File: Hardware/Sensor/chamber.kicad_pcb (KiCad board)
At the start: 2 copper layers, 83 x 95 mm, 106 parts, among them J1 Conn_01x16_Female, J2 Conn_01x16_Female, J3 RF_Shield_One_Piece, J4 Conn_Coaxial, J5 Conn_01x03_Male, J6 Conn_01x03_Male, J7 UART, J8 USB_B_Micro, J9 Conn_01x04, Q1 Q_PMOS_GDS, Q2 Q_PMOS_GDS, Q3 Q_NMOS_GDS, Q4 Q_NMOS_GDS, Q5 Q_NPN_BEC, Q6 Q_PMOS_GDS, Q7 Q_NMOS_GDS, Q8 Q_PMOS_GDS, Q9 Q_NMOS_GDS, SW1 UP, SW2 DOWN, SW3 LEFT, SW4 RIGHT, U1 SSD1306, U2 MCP3425A0T-ECH, U3 LMC662, U4 LM358, U5 STM8S105K4B6, Y1 Crystal

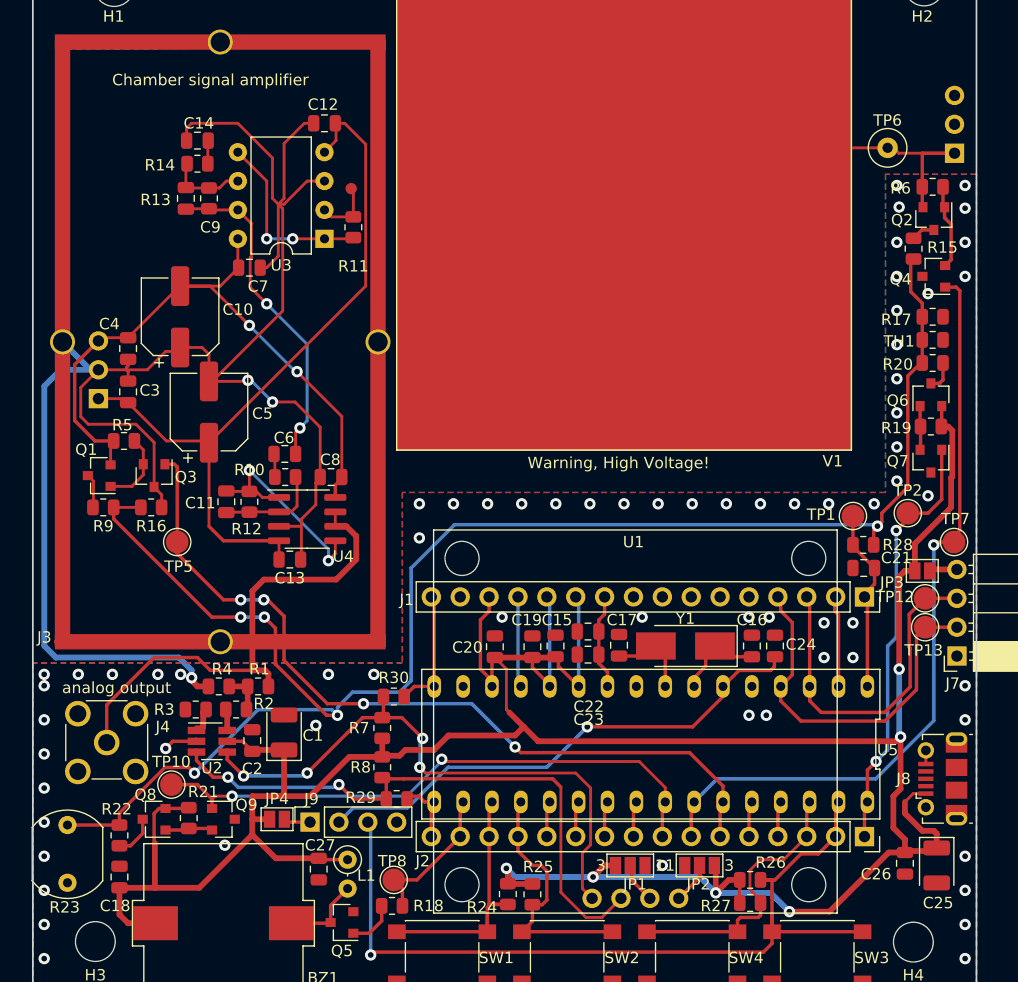
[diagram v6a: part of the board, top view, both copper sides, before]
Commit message: added references to LCSC shop (for some components), slighty improved routing
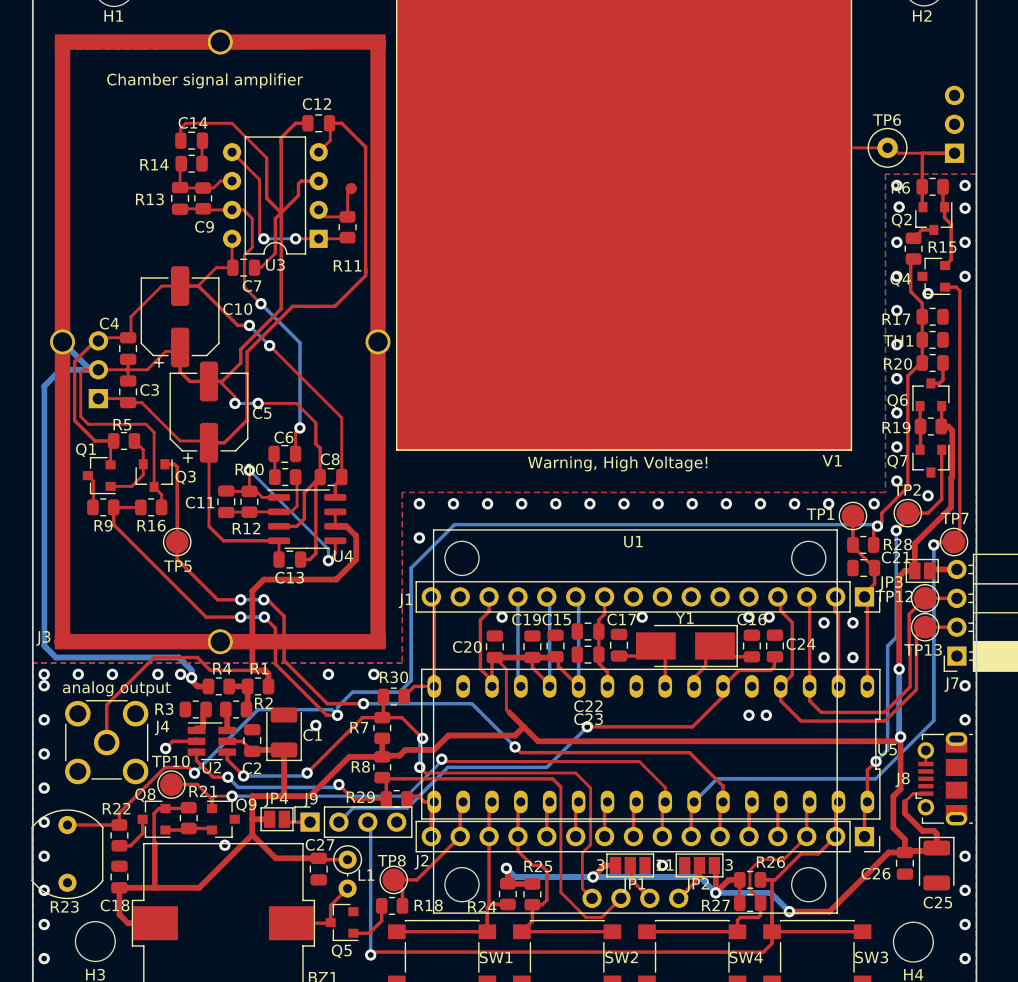
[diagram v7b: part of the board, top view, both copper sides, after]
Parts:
- moved C9 0.51 mm to (70.0, 48.1)
- moved C12 0.51 mm to (82.1, 41.5)
- moved C14 0.51 mm to (71.0, 43.1)
- moved C7 0.51 mm to (75.5, 54.2)
- moved R11 0.51 mm to (84.7, 50.7)
- moved R13 0.51 mm to (72.0, 48.1)
- moved R14 0.51 mm to (71.0, 45.1)
- moved U3 0.51 mm to (82.1, 51.7)
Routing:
- net GND: track 286.7 -> 295.2 mm
- net -BATT: track 65.4 -> 69.1 mm
- net +BATT: track 58.2 -> 59.1 mm
- net Net-(C6-Pad1): track 29.3 -> 30.0 mm

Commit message: cleanup after transition to KiCad6
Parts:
- R18: value 10k -> 1k
- R24, R25, R26, R27: value TBD -> 1k
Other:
- net class Default removed
- net class high voltage removed
